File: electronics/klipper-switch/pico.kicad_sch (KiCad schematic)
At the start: 0 parts

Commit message: created schematic pages
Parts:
- added U1: Pico, RPi_Pico:RPi_Pico_SMD_TH, symbol klipper-switch:Pico
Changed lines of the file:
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@@
 	(generator_version "8.0")
 	(paper "A4")
+	(symbol
+		(lib_id "klipper-switch:Pico")
+		(at 77.47 97.79 0)
+		(unit 1)
+		(exclude_from_sim no)
+		(in_bom yes)
+		(on_board yes)
+		(dnp no)
+		(fields_autoplaced yes)
+		(property "Reference" "U1"
+			(at 77.47 66.04 0)
+			(effects
+				(font
+					(size 1.27 1.27)
+				)
+			)
+		)
+		(property "Value" "Pico"
+			(at 77.47 68.58 0)
+			(effects
+				(font
+					(size 1.27 1.27)
+				)
+			)
+		)
+		(property "Footprint" "RPi_Pico:RPi_Pico_SMD_TH"
+			(at 77.47 97.79 90)
+			(effects
+				(font
+					(size 1.27 1.27)
+				)
+				(hide yes)
+			)
+		)
+		(property "Datasheet" "https://datasheets.raspberrypi.com/pico/pico-datasheet.pdf"
+			(at 77.47 97.79 0)
+			(effects
+				(font
+					(size 1.27 1.27)
+				)
+				(hide yes)
+			)
+		)
+		(property "Description" "RP2040 Raspberry Pi Pico - ARM® Cortex®-M0+ MCU 32-Bit Embedded Evaluation Board"
+			(at 77.47 97.79 0)
+			(effects
+				(font
+					(size 1.27 1.27)
+				)
+				(hide yes)
+			)
+		)
+		(property "Manufacturer#" "2648-SC0915TR-ND"
+			(at 77.47 97.79 0)
+			(effects
+				(font
+					(size 1.27 1.27)
+				)
+				(hide yes)
+			)
+		)
+		(property "Supplier#" "2648-SC0915TR-ND"
+			(at 77.47 97.79 0)
+			(effects
+				(font
+					(size 1.27 1.27)
+				)
+				(hide yes)
+			)
+		)
+		(property "Supplier" "Digikey Electronics, Inc."
+			(at 77.47 97.79 0)
+			(effects
+				(font
+					(size 1.27 1.27)
+				)
+				(hide yes)
+			)
+		)
+		(property "Role" "MCU"
+			(at 77.47 97.79 0)
+			(effects
+				(font
+					(size 1.27 1.27)
+				)
+				(hide yes)
+			)
+		)
+		(property "Manufacturer" "Raspberry Pi"
+			(at 77.47 97.79 0)
+			(effects
+				(font
+					(size 1.27 1.27)
+				)
+				(hide yes)
+			)
+		)
+		(pin "10"
+		)
+		(pin "14"
+		)
+		(pin "15"
+		)
+		(pin "18"
+		)
+		(pin "1"
+		)
+		(pin "41"
+		)
+		(pin "42"
+		)
+		(pin "43"
+		)
+		(pin "5"
+		)
+		(pin "4"
+		)
+		(pin "40"
+		)
+		(pin "16"
+		)
+		(pin "25"
+		)
+		(pin "26"
+		)
+		(pin "29"
+		)
+		(pin "3"
+		)
+		(pin "6"
+		)
+		(pin "7"
+		)
+		(pin "12"
+		)
+		(pin "13"
+		)
+		(pin "21"
+		)
+		(pin "22"
+		)
+		(pin "34"
+		)
+		(pin "35"
+		)
+		(pin "38"
+		)
+		(pin "39"
+		)
+		(pin "30"
+		)
+		(pin "31"
+		)
+		(pin "23"
+		)
+		(pin "24"
+		)
+		(pin "17"
+		)
+		(pin "8"
+		)
+		(pin "9"
+		)
+		(pin "32"
+		)
+		(pin "33"
+		)
+		(pin "20"
+		)
+		(pin "27"
+		)
+		(pin "28"
+		)
+		(pin "11"
+		)
+		(pin "2"
+		)
+		(pin "36"
+		)
+		(pin "37"
+		)
+		(pin "19"
+		)
+		(instances
+			(project ""
+				(path "/e5df92b1-e048-41e8-96e5-ed9a12dbef0e/8040985a-5eaa-4ffd-a81f-f30f9f1fb608"
+					(reference "U1")
+					(unit 1)
+				)
+			)
+		)
+	)
 )

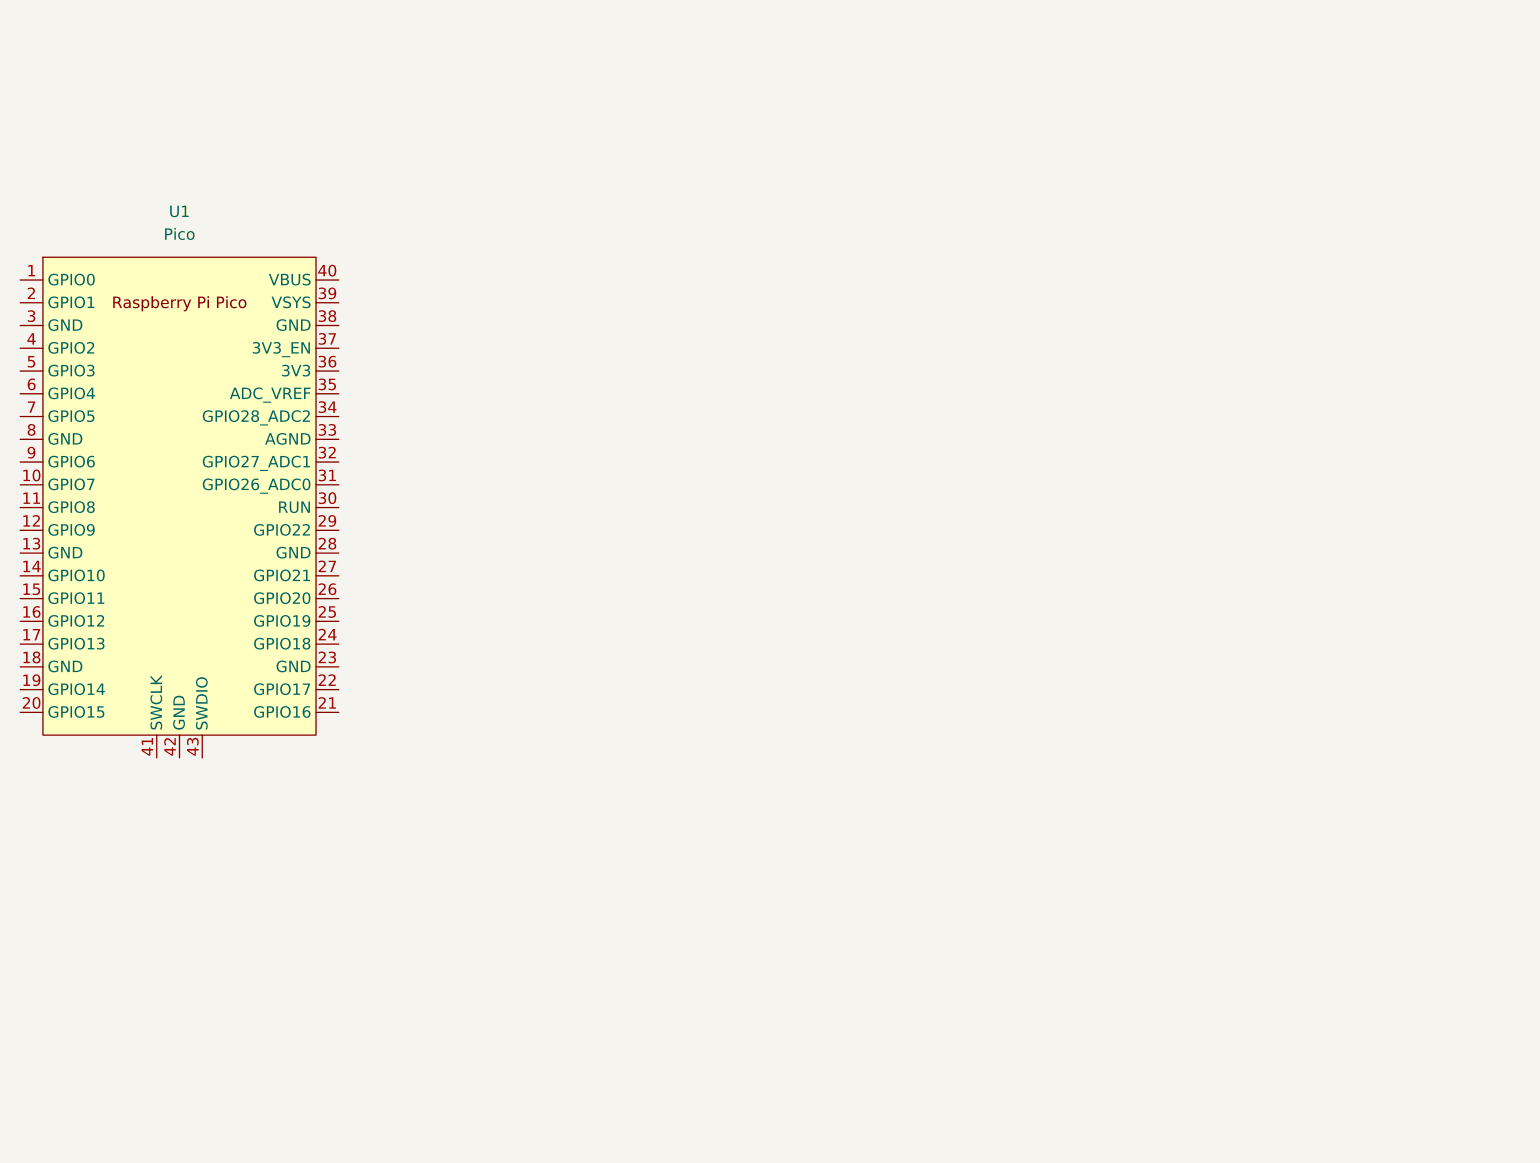
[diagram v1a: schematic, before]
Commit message: schematic naming and pico symbol update
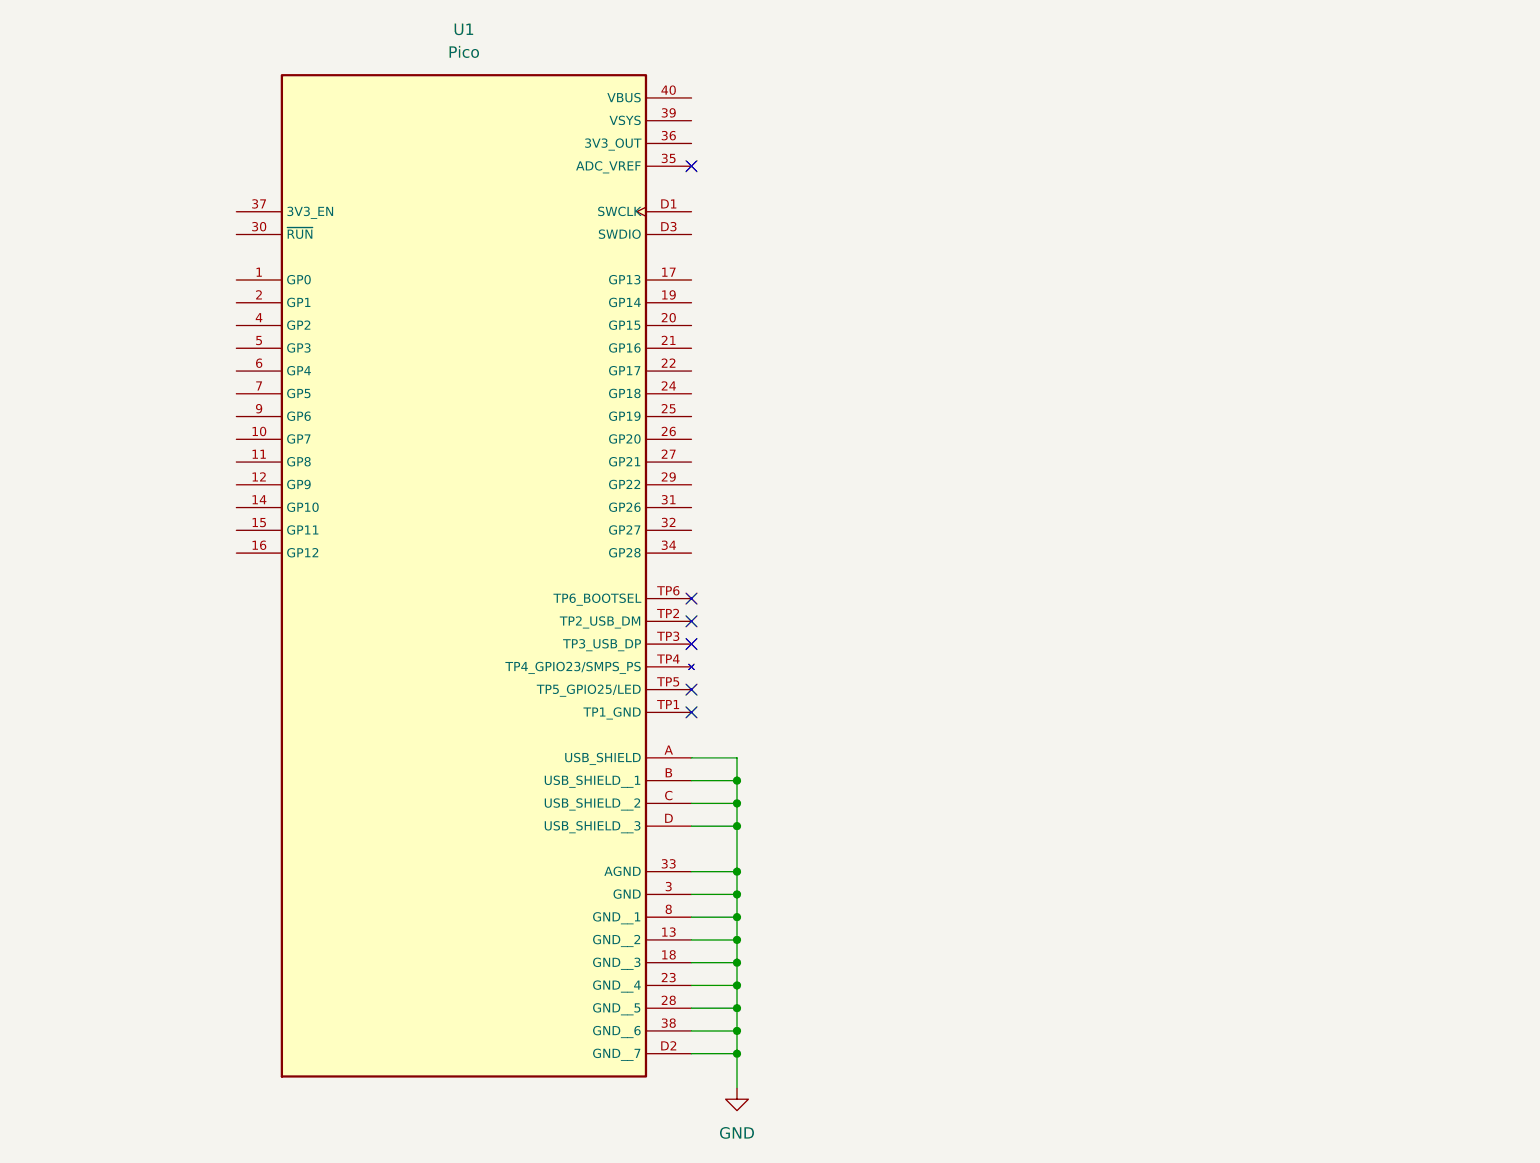
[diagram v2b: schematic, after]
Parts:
- U1: footprint RPi_Pico:RPi_Pico_SMD_TH -> klipper-switch:pico
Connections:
- net GND: now reaches U1.13 (GND__2)
- net GND: now also U1.18 (GND__3), U1.23 (GND__4), U1.28 (GND__5), U1.3 (GND), U1.33 (AGND), U1.38 (GND__6), U1.8 (GND__1), U1.A (USB_SHIELD), U1.B (USB_SHIELD__1), U1.C (USB_SHIELD__2), U1.D (USB_SHIELD__3), U1.D2 (GND__7)
- no-connect marks 0 -> 6
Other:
- title: (none) -> klipper-switch, pico

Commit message: LEDs & Molex CONNs
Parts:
- added J2: Conn_01x04_Pin, Connector_PinHeader_2.54mm:PinHeader_1x04_P2.54mm_Vertical, symbol Connector:Conn_01x04_Pin
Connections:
- net GND: now also J2.1 (Pin_1)
- net VBUS: now reaches U1.40 (VBUS)
- net VBUS: now also J2.2 (Pin_2)
- net SWCLK: now reaches U1.D1 (SWCLK)
- net SWCLK: now also J2.4 (Pin_4)
- net SWDIO: now reaches U1.D3 (SWDIO)
- net SWDIO: now also J2.3 (Pin_3)
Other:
- note added: "DEBUGGING"

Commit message: completed rough schematic
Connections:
- net GPIO_00: now reaches U1.1 (GP0)
- net GPIO_07: now reaches U1.10 (GP7)
- net GPIO_08: now reaches U1.11 (GP8)
- net GPIO_09: now reaches U1.12 (GP9)
- net GPIO_10: now reaches U1.14 (GP10)
- net GPIO_11: now reaches U1.15 (GP11)
- net GPIO_12: now reaches U1.16 (GP12)
- net GPIO_13: now reaches U1.17 (GP13)
- net GPIO_14: now reaches U1.19 (GP14)
- net GPIO_01: now reaches U1.2 (GP1)
- net GPIO_15: now reaches U1.20 (GP15)
- net GPIO_16: now reaches U1.21 (GP16)
- net GPIO_17: now reaches U1.22 (GP17)
- net GPIO_18: now reaches U1.24 (GP18)
- net GPIO_19: now reaches U1.25 (GP19)
- net GPIO_20: now reaches U1.26 (GP20)
- net GPIO_21: now reaches U1.27 (GP21)
- net GPIO_22: now reaches U1.29 (GP22)
- net GPIO_23: now reaches U1.31 (GP26)
- net +3.3V: now reaches U1.36 (3V3_OUT)
- net GPIO_02: now reaches U1.4 (GP2)
- net GPIO_03: now reaches U1.5 (GP3)
- net GPIO_04: now reaches U1.6 (GP4)
- net GPIO_05: now reaches U1.7 (GP5)
- net GPIO_06: now reaches U1.9 (GP6)
- no-connect marks 6 -> 11
